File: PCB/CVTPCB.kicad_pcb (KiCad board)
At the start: 2 copper layers, 72 x 92.5 mm, 16 parts, among them J1 PrimaryPads, J3 SecondaryPads, J4 12V_5V_Regulator, J7 SystemInput

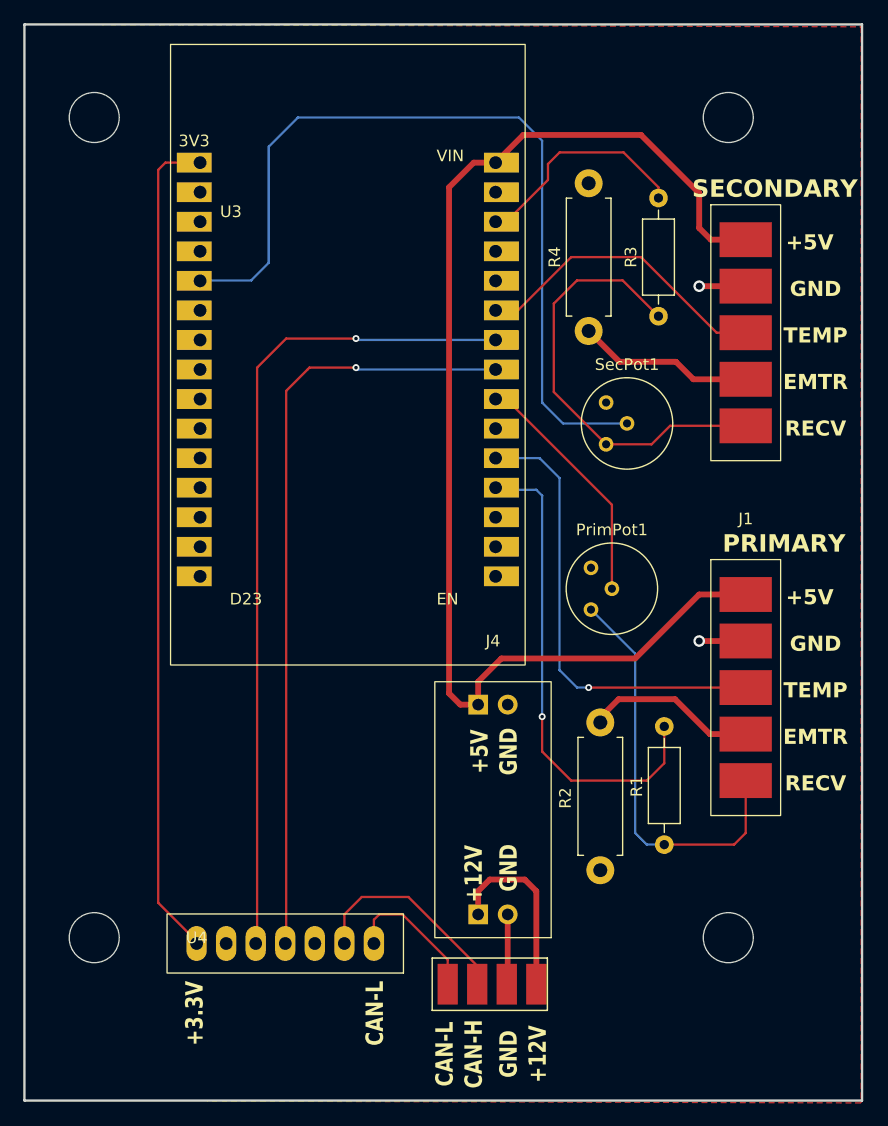
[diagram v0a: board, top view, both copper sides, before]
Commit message: Partial fix for incorrect voltage divider
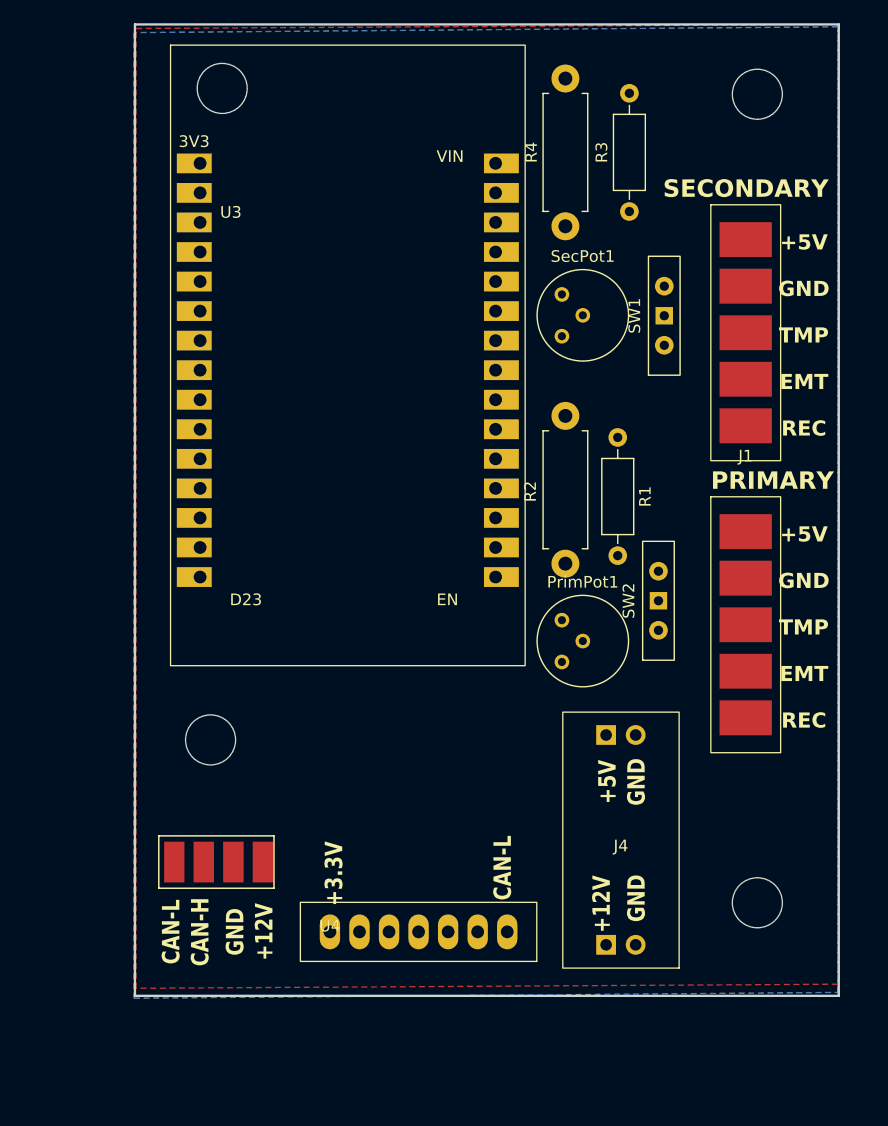
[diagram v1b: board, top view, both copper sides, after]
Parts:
- added SW1: SW_SPDT, Button_Switch_THT:SW_Slide-03_Wuerth-WS-SLTV_10x2.5x6.4_P2.54mm, F.Cu at (155.0, 77.5)
- added SW2: SW_SPDT, Button_Switch_THT:SW_Slide-03_Wuerth-WS-SLTV_10x2.5x6.4_P2.54mm, F.Cu at (154.5, 102.0)
- moved R1 35.2 mm to (151.0, 88.0), turned to -90 degrees
- moved R2 26.5 mm to (146.5, 86.2)
- moved J7 25.7 mm to (116.5, 124.5)
- moved H2 19.7 mm to (116.0, 114.0)
- moved U4 11.5 mm to (126.3, 130.5)
- moved J4 11.3 mm to (151.3, 108.6)
- moved H4 11.3 mm to (117.0, 58.0)
- moved SecPot1 10.0 mm to (146.2, 79.3)
- moved R3 9.34 mm to (152.0, 68.6)
- moved R4 9.22 mm to (146.5, 69.8)
- moved J1 5.40 mm to (162.0, 90.1)
- moved PrimPot1 5.15 mm to (146.2, 107.3)
- moved H1 3.91 mm to (163.0, 128.0)
- moved H3 3.20 mm to (163.0, 58.5)
- moved U3 0.06 mm to (127.8, 64.4)
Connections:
- PrimPot1 pad 1: Net-(J1-Pin_5) -> Net-(SW2-C)
- PrimPot1 pad 2: Net-(U3-D33) -> GND
- PrimPot1 pad 3: GND -> unconnected-(PrimPot1-Pad3)
- R1 pad 1: Net-(J1-Pin_5) -> Net-(SW2-A)
- R1 pad 2: Net-(U3-D34) -> GND
- R3 pad 1: Net-(J3-Pin_5) -> Net-(SW1-A)
- R3 pad 2: Net-(U3-D13) -> GND
- SecPot1 pad 1: Net-(J3-Pin_5) -> Net-(SW1-C)
- SecPot1 pad 2: Net-(U3-D4) -> GND
- SecPot1 pad 3: GND -> unconnected-(SecPot1-Pad3)
- U3 pad 19: Net-(U3-D34) -> Net-(SW2-A)
- U3 pad 22: Net-(U3-D33) -> Net-(SW2-C)
- U3 pad 28: Net-(U3-D13) -> Net-(SW1-A)
- U3 pad 5: Net-(U3-D4) -> Net-(SW1-C)
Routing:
- net +5V: track 107.3 -> 0.00 mm
- net Net-(U3-D4): track 72.4 -> 0.00 mm
- net +3.3V: track 71.7 -> 0.00 mm
- net Net-(U3-D26): track 71.4 -> 0.00 mm, vias 1 -> 0
- net Net-(U3-D25): track 66.5 -> 0.00 mm, vias 1 -> 0
- net Net-(U3-D34): track 41.6 -> 0.00 mm, vias 1 -> 0
- net Net-(J1-Pin_3): track 39.3 -> 0.00 mm, vias 1 -> 0
- net Net-(J3-Pin_5): track 37.7 -> 0.00 mm
- net Net-(J1-Pin_5): track 35.6 -> 0.00 mm
- net Net-(J3-Pin_3): track 26.1 -> 0.00 mm
- net Net-(U3-D33): track 21.0 -> 0.00 mm
- net Net-(U3-D13): track 19.4 -> 0.00 mm
- net Net-(J7-Pin_3): track 18.6 -> 0.00 mm
- net Net-(J4-Pin_3): track 15.8 -> 0.00 mm
- net Net-(J3-Pin_4): track 15.2 -> 0.00 mm
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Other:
- board size 72 x 92.5 mm -> 60.5 x 83.5 mm
- board text added: "EMT"
- board text added: "REC"
- board text added: "TMP"
- board text removed: "EMTR"
- board text removed: "RECV"
- board text removed: "TEMP"

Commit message: Complete pot/resistor issue fix
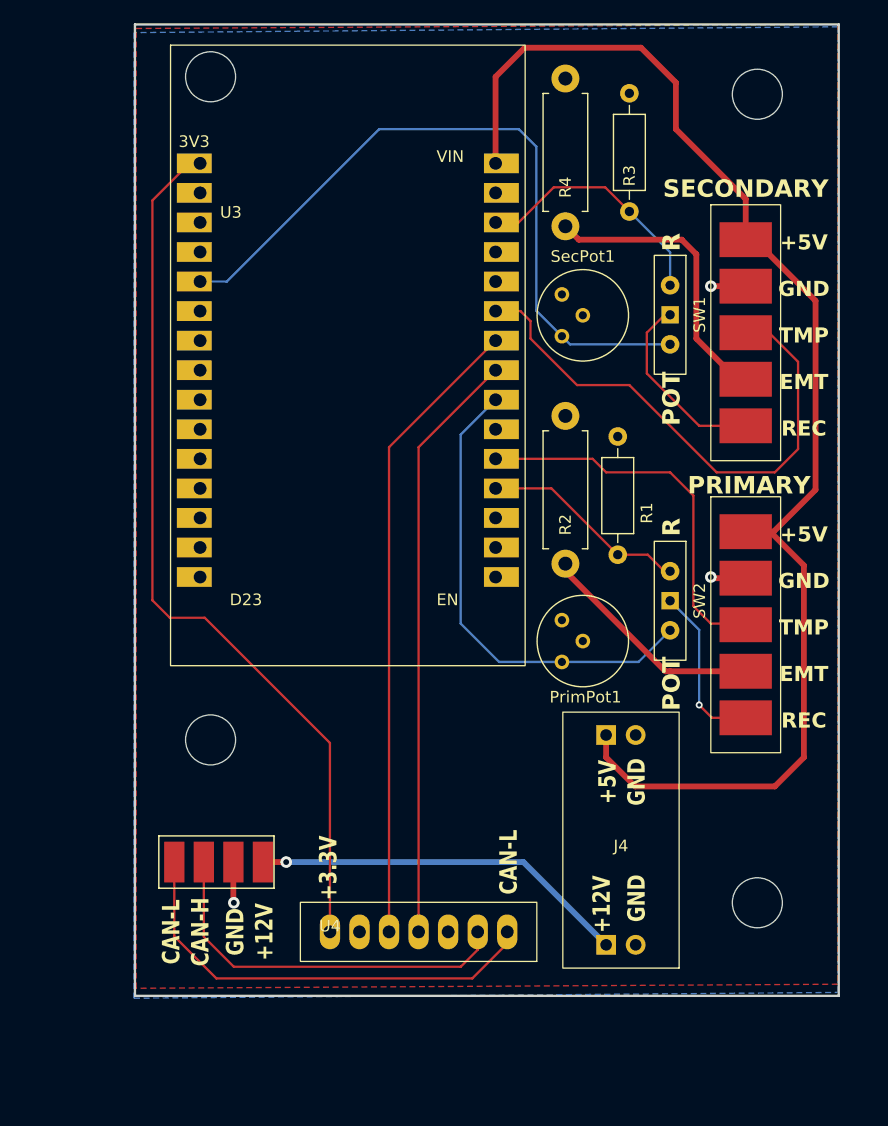
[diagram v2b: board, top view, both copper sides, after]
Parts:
- moved R2 12.7 mm to (146.5, 98.8), turned to 90 degrees
- moved R1 10.1 mm to (151.0, 98.1), turned to 90 degrees
- moved H4 1.41 mm to (116.0, 57.0)
- moved SW2 1.00 mm to (155.5, 102.0), turned to -90 degrees
- moved SW1 0.51 mm to (155.5, 77.5), turned to -90 degrees
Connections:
- SW1 pad 1: Net-(SW1-A) -> Net-(J3-Pin_5)
- SW1 pad 2: Net-(J3-Pin_5) -> Net-(SW1-A)
- SW2 pad 1: Net-(SW2-A) -> Net-(J1-Pin_5)
- SW2 pad 2: Net-(J1-Pin_5) -> Net-(SW2-A)
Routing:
- net +5V: track 0.00 -> 116.8 mm
- net +3.3V: track 0.00 -> 76.4 mm
- net Net-(SW1-C): track 0.00 -> 61.7 mm
- net Net-(U3-D26): track 0.00 -> 54.6 mm
- net Net-(U3-D25): track 0.00 -> 51.0 mm
- net Net-(J3-Pin_3): track 0.00 -> 46.5 mm
- net Net-(SW2-C): track 0.00 -> 41.0 mm
- net Net-(J7-Pin_4): track 0.00 -> 38.7 mm
- net Net-(J7-Pin_3): track 0.00 -> 33.2 mm
- net Net-(J1-Pin_3): track 0.00 -> 33.0 mm
- net Net-(J4-Pin_3): track 0.00 -> 32.4 mm, vias 0 -> 1
- net Net-(J3-Pin_4): track 0.00 -> 25.2 mm
- net Net-(SW1-A): track 0.00 -> 21.4 mm
- net Net-(J1-Pin_4): track 0.00 -> 20.3 mm
- net Net-(SW2-A): track 0.00 -> 17.9 mm
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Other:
- board text added: "POT"
- board text added: "R"
- board text removed: "12+"

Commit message: Update to new PCB
This PCB features comparators with hysteresis added, surface mount hardware for voltage regulation and CAN protocol, and numerous test points for debugging
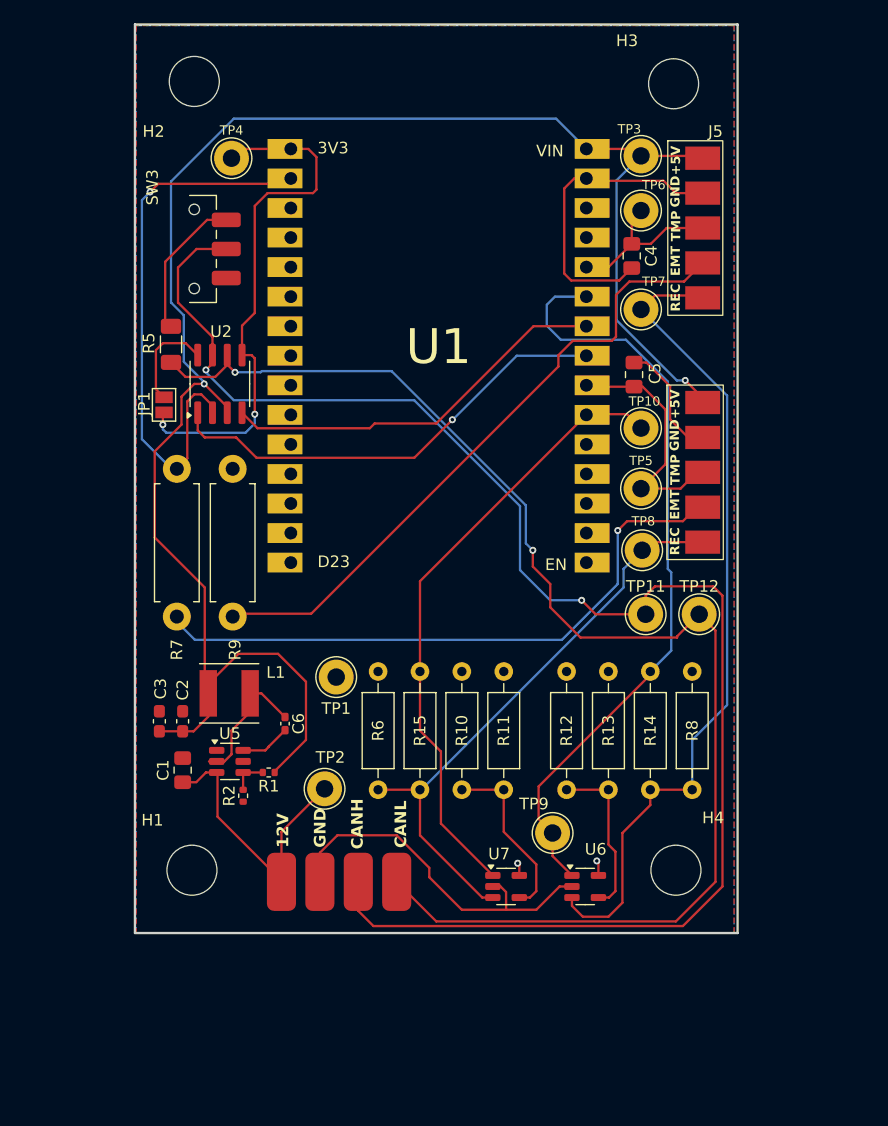
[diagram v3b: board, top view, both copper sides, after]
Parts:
- removed J1: PrimaryPads, CVT:Temp_IR_5_Pad_Combo
- removed J3: SecondaryPads, CVT:Temp_IR_5_Pad_Combo
- removed J4: 12V_5V_Regulator, CVT:PowerBoard
- removed J7: SystemInput, CVT:JST4Pin
- removed PrimPot1, SecPot1: 0-10k, Potentiometer_THT:Potentiometer_Bourns_3339H_Vertical
- removed R3: R, Resistor_THT:R_Axial_DIN0207_L6.3mm_D2.5mm_P10.16mm_Horizontal
- removed R4: 22, Resistor_THT:R_Axial_DIN0411_L9.9mm_D3.6mm_P12.70mm_Horizontal
- removed SW1, SW2: SW_SPDT, Button_Switch_THT:SW_Slide-03_Wuerth-WS-SLTV_10x2.5x6.4_P2.54mm
- removed U3: ~, CVT:ESP 32 BAJA
- removed U4: ~, CVT:1x7 Connectors
- added C1: 10u, Capacitor_SMD:C_0805_2012Metric_Pad1.18x1.45mm_HandSolder, F.Cu at (113.6, 116.6)
- added C2: 22u, Capacitor_SMD:C_0603_1608Metric_Pad1.08x0.95mm_HandSolder, F.Cu at (113.6, 112.4)
- added C3: 22u, Capacitor_SMD:C_0603_1608Metric_Pad1.08x0.95mm_HandSolder, F.Cu at (111.6, 112.4)
- added C4: C, Capacitor_SMD:C_0805_2012Metric_Pad1.18x1.45mm_HandSolder, F.Cu at (152.2, 72.4)
- added C5: C, Capacitor_SMD:C_0805_2012Metric_Pad1.18x1.45mm_HandSolder, F.Cu at (152.4, 82.6)
- added C6: 100n, Capacitor_SMD:C_0402_1005Metric_Pad0.74x0.62mm_HandSolder, F.Cu at (122.4, 112.6)
- added J2: SecondaryPads, CVT:Temp_IR_5_Pad_Combo, F.Cu at (157.8, 80.5)
- added J5: PrimaryPads, CVT:Temp_IR_5_Pad_Combo, F.Cu at (158.3, 59.5)
- added J6: ~, NJIT-Baja-Footprints:Aviation Plug Pads, F.Cu at (122.1, 126.2)
- added JP1: Jumper_2_Open, Jumper:SolderJumper-2_P1.3mm_Open_Pad1.0x1.5mm, F.Cu at (112.0, 85.2)
- added L1: 3.3u, Inductor_SMD:L_Taiyo-Yuden_NR-50xx, F.Cu at (117.6, 110.0)
- added R10: R, Resistor_THT:R_Axial_DIN0207_L6.3mm_D2.5mm_P10.16mm_Horizontal, F.Cu at (137.6, 118.3)
- added R11: R, Resistor_THT:R_Axial_DIN0207_L6.3mm_D2.5mm_P10.16mm_Horizontal, F.Cu at (141.2, 108.1)
- added R12: R, Resistor_THT:R_Axial_DIN0207_L6.3mm_D2.5mm_P10.16mm_Horizontal, F.Cu at (146.6, 118.3)
- added R13: R, Resistor_THT:R_Axial_DIN0207_L6.3mm_D2.5mm_P10.16mm_Horizontal, F.Cu at (150.2, 108.1)
- added R14: R, Resistor_THT:R_Axial_DIN0207_L6.3mm_D2.5mm_P10.16mm_Horizontal, F.Cu at (153.8, 108.1)
- added R15: R, Resistor_THT:R_Axial_DIN0207_L6.3mm_D2.5mm_P10.16mm_Horizontal, F.Cu at (134.0, 108.1)
- added R5: 120, Resistor_SMD:R_1206_3216Metric_Pad1.30x1.75mm_HandSolder, F.Cu at (112.6, 80.0)
- added R6: R, Resistor_THT:R_Axial_DIN0207_L6.3mm_D2.5mm_P10.16mm_Horizontal, F.Cu at (130.4, 108.1)
- added R7: 47, Resistor_THT:R_Axial_DIN0411_L9.9mm_D3.6mm_P12.70mm_Horizontal, F.Cu at (113.1, 103.4)
- added R8: R, Resistor_THT:R_Axial_DIN0207_L6.3mm_D2.5mm_P10.16mm_Horizontal, F.Cu at (157.4, 108.1)
- added R9: 47, Resistor_THT:R_Axial_DIN0411_L9.9mm_D3.6mm_P12.70mm_Horizontal, F.Cu at (117.9, 103.4)
- added SW3: SW_SPDT, Button_Switch_SMD:SW_SPDT_CK_JS102011SAQN, F.Cu at (114.6, 71.8)
- added TP1: TestPoint, TestPoint:TestPoint_THTPad_D3.0mm_Drill1.5mm, F.Cu at (126.8, 108.6)
- added TP10: TestPoint, TestPoint:TestPoint_THTPad_D3.0mm_Drill1.5mm, F.Cu at (153.0, 87.2)
- added TP11: TestPoint, TestPoint:TestPoint_THTPad_D3.0mm_Drill1.5mm, F.Cu at (153.4, 103.2)
- added TP12: TestPoint, TestPoint:TestPoint_THTPad_D3.0mm_Drill1.5mm, F.Cu at (158.0, 103.2)
- added TP2: TestPoint, TestPoint:TestPoint_THTPad_D3.0mm_Drill1.5mm, F.Cu at (125.8, 118.2)
- added TP3: TestPoint, TestPoint:TestPoint_THTPad_D3.0mm_Drill1.5mm, F.Cu at (153.0, 63.8)
- added TP4: TestPoint, TestPoint:TestPoint_THTPad_D3.0mm_Drill1.5mm, F.Cu at (117.8, 64.0)
- added TP5: TestPoint, TestPoint:TestPoint_THTPad_D3.0mm_Drill1.5mm, F.Cu at (153.0, 92.4)
- added TP6: TestPoint, TestPoint:TestPoint_THTPad_D3.0mm_Drill1.5mm, F.Cu at (153.0, 68.5)
- added TP7: TestPoint, TestPoint:TestPoint_THTPad_D3.0mm_Drill1.5mm, F.Cu at (153.0, 77.0)
- added TP8: TestPoint, TestPoint:TestPoint_THTPad_D3.0mm_Drill1.5mm, F.Cu at (153.1, 97.7)
- added TP9: TestPoint, TestPoint:TestPoint_THTPad_D3.0mm_Drill1.5mm, F.Cu at (145.4, 122.0)
- added U1: ESP32, NJIT-Baja-Footprints:ESP32, F.Cu at (135.6, 63.2)
- added U2: TJA1051T-3, Package_SO:SOIC-8_3.9x4.9mm_P1.27mm, F.Cu at (116.8, 83.4)
- added U5: AP62301WU, Package_TO_SOT_SMD:TSOT-23-6, F.Cu at (117.7, 115.8)
- added U6: MCP6561-OT, Package_TO_SOT_SMD:SOT-23-5, F.Cu at (148.2, 126.6)
- added U7: MCP6561-OT, Package_TO_SOT_SMD:SOT-23-5, F.Cu at (141.4, 126.6)
- R1: value R -> 52.3k; footprint Resistor_THT:R_Axial_DIN0207_L6.3mm_D2.5mm_P10.16mm_Horizontal -> Resistor_SMD:R_0402_1005Metric
- R2: value 22 -> 10k; footprint Resistor_THT:R_Axial_DIN0411_L9.9mm_D3.6mm_P12.70mm_Horizontal -> Resistor_SMD:R_0402_1005Metric
- moved H4 79.1 mm to (156.0, 125.2)
- moved H2 56.6 mm to (114.6, 57.4)
- moved H1 48.7 mm to (114.4, 125.2)
- moved R1 35.4 mm to (121.0, 116.8), turned to 180 degrees
- moved R2 34.1 mm to (118.8, 118.8), turned to -90 degrees
- moved H3 7.26 mm to (155.8, 57.6)
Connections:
- R1 pad 1: Net-(SW2-A) -> +5V
- R1 pad 2: GND -> Net-(U5-FB)
- R2 pad 1: Net-(J1-Pin_4) -> Net-(U5-FB)
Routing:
- net Net-(J6-CANH): track 0.00 -> 135.6 mm, vias 0 -> 2
- net Net-(J6-CANL): track 0.00 -> 116.4 mm, vias 0 -> 2
- net GND: track 9.56 -> 116.1 mm, vias 3 -> 1
- net Net-(J5-Pin_5): track 0.00 -> 73.1 mm
- net Net-(U1-D27): track 0.00 -> 66.9 mm
- net Net-(SW1-C): track 61.7 -> 0.00 mm
- net Net-(J5-Pin_4): track 0.00 -> 55.7 mm
- net Net-(U3-D26): track 54.6 -> 0.00 mm
- net Net-(U1-D32): track 0.00 -> 53.3 mm
- net Net-(J2-Pin_4): track 0.00 -> 53.2 mm, vias 0 -> 1
- net Net-(U3-D25): track 51.0 -> 0.00 mm
- net Net-(J2-Pin_5): track 0.00 -> 49.6 mm
- net Net-(J3-Pin_3): track 46.5 -> 0.00 mm
- net Net-(SW2-C): track 41.0 -> 0.00 mm
- net Net-(U1-D25): track 0.00 -> 39.5 mm, vias 0 -> 1
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- added copper zone on B.Cu, net +3.3V
- added copper zone on F.Cu, net GND
- removed copper zone on F.Cu, net (none)
- removed copper zone on B.Cu, net GND
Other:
- board size 60.5 x 83.5 mm -> 51.8 x 78.1 mm
- board text removed: "+12V"
- board text removed: "+3.3V"
- board text removed: "+5V"
- board text removed: "CAN-H"
- board text removed: "CAN-L"
- board text removed: "EMT"
- board text removed: "GND"
- board text removed: "POT"
- board text removed: "PRIMARY"
- board text removed: "R"
- board text removed: "REC"
- board text removed: "SECONDARY"
- board text removed: "TMP"

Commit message: Update PCB to use comparator, includes new GBR and DRL
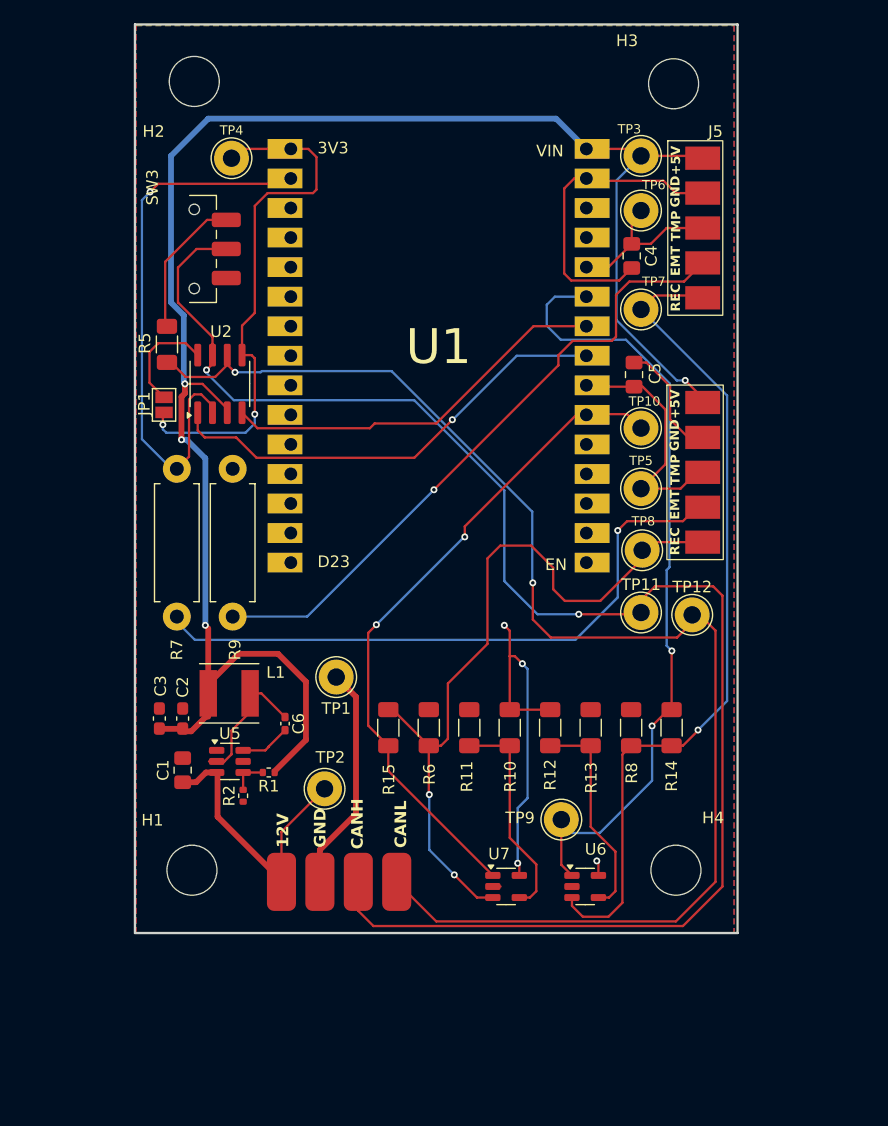
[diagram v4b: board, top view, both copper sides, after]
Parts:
- R10, R11, R12, R13, R14, R15, R6, R8: footprint Resistor_THT:R_Axial_DIN0207_L6.3mm_D2.5mm_P10.16mm_Horizontal -> Resistor_SMD:R_1206_3216Metric_Pad1.30x1.75mm_HandSolder
- moved R8 7.13 mm to (152.2, 113.0)
- moved R10 6.73 mm to (141.7, 113.0)
- moved R6 6.50 mm to (134.8, 113.0)
- moved R11 5.67 mm to (138.2, 113.0)
- moved R15 5.54 mm to (131.3, 113.0), turned to 90 degrees
- moved R12 5.51 mm to (145.2, 113.0)
- moved R14 5.16 mm to (155.6, 113.0)
- moved R13 5.07 mm to (148.7, 113.0)
- moved TP9 1.37 mm to (146.2, 120.8)
- moved TP12 0.60 mm to (157.4, 103.2)
- moved TP11 0.43 mm to (153.0, 103.0)
- moved R5 0.35 mm to (112.2, 80.0)
- moved C2 0.24 mm to (113.6, 112.2)
- moved C3 0.24 mm to (111.6, 112.2)
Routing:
- net +3.3V: track 48.9 -> 78.9 mm, vias 4 -> 6
- net Net-(J2-Pin_5): track 49.6 -> 63.7 mm, vias 0 -> 2
- net GND: track 116.1 -> 105.4 mm
- net Net-(U6--): track 14.3 -> 18.6 mm
- net Net-(U1-D32): track 53.3 -> 57.6 mm, vias 0 -> 2
- net Net-(U7--): track 15.2 -> 18.6 mm
- net Net-(U1-D27): track 66.9 -> 69.6 mm, vias 0 -> 2
- net Net-(J6-CANL): track 116.4 -> 118.2 mm
- net Net-(J6-CANH): track 135.6 -> 136.8 mm
- net Net-(JP1-B): track 8.61 -> 9.30 mm
- net Net-(J2-Pin_4): track 53.2 -> 53.9 mm
- net Net-(J5-Pin_5): track 73.1 -> 73.6 mm, vias 0 -> 1
- net Net-(J5-Pin_4): track 55.7 -> 56.0 mm, vias 0 -> 1
- net +5V: track 154.5 -> 154.4 mm, vias 2 -> 4
